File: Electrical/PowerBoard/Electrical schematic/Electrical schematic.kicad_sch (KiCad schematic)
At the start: 8 parts, among them J1 S4B-XH-SM4-TB, J2 XT60PW-M, J3 XT60PW-M, J4 2171750001, J5 XT60PW-M, U4 TMUX1204DGSR

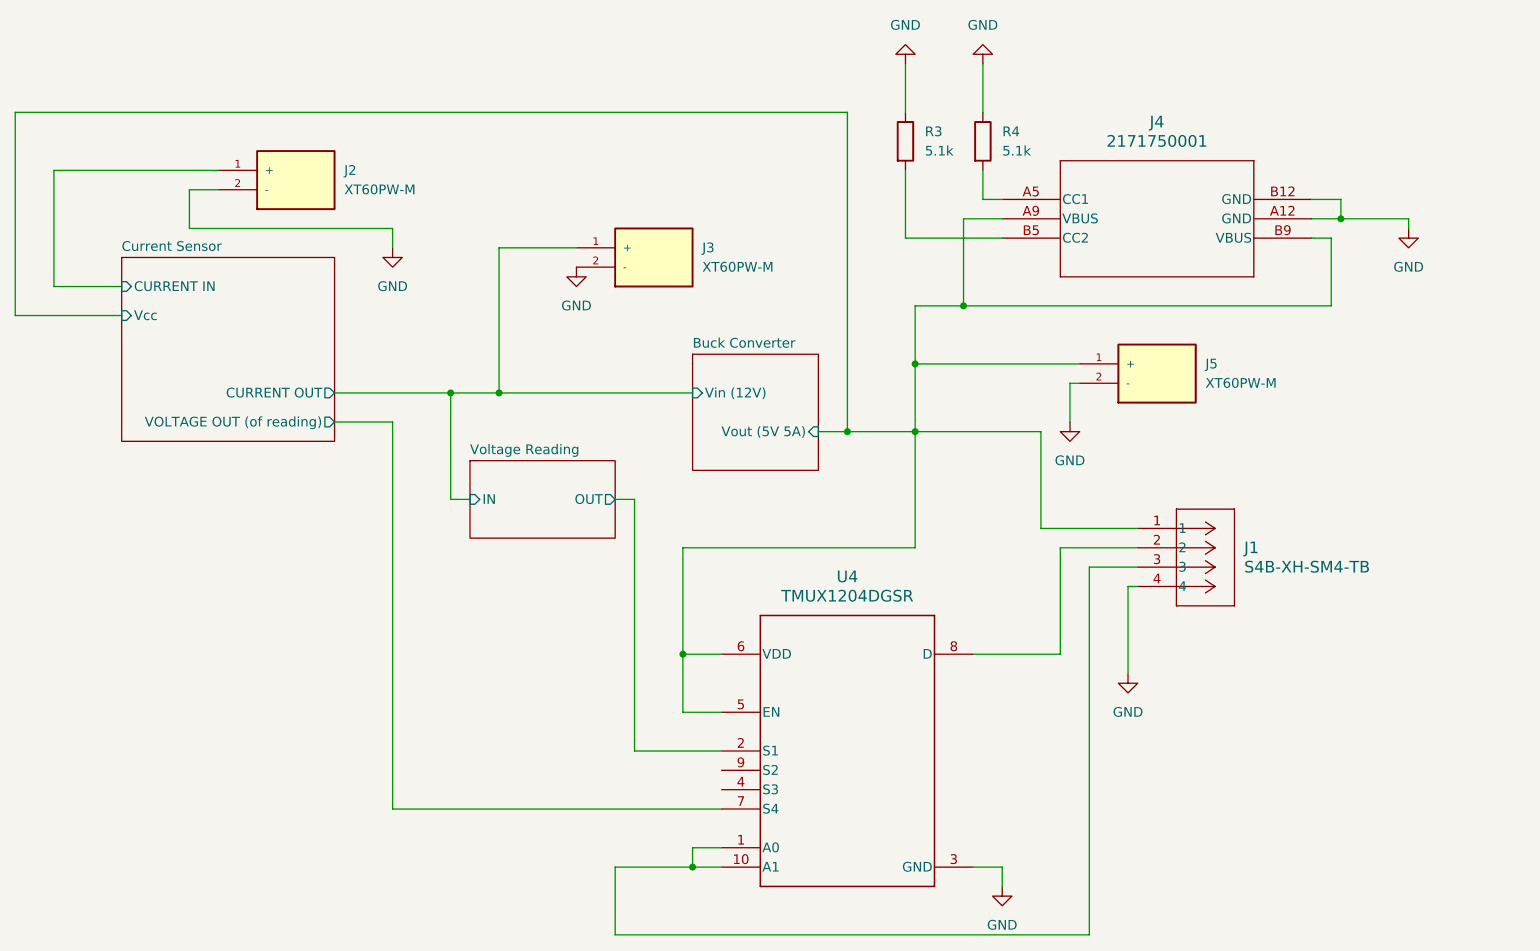
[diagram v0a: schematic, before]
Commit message: new mux/usbA
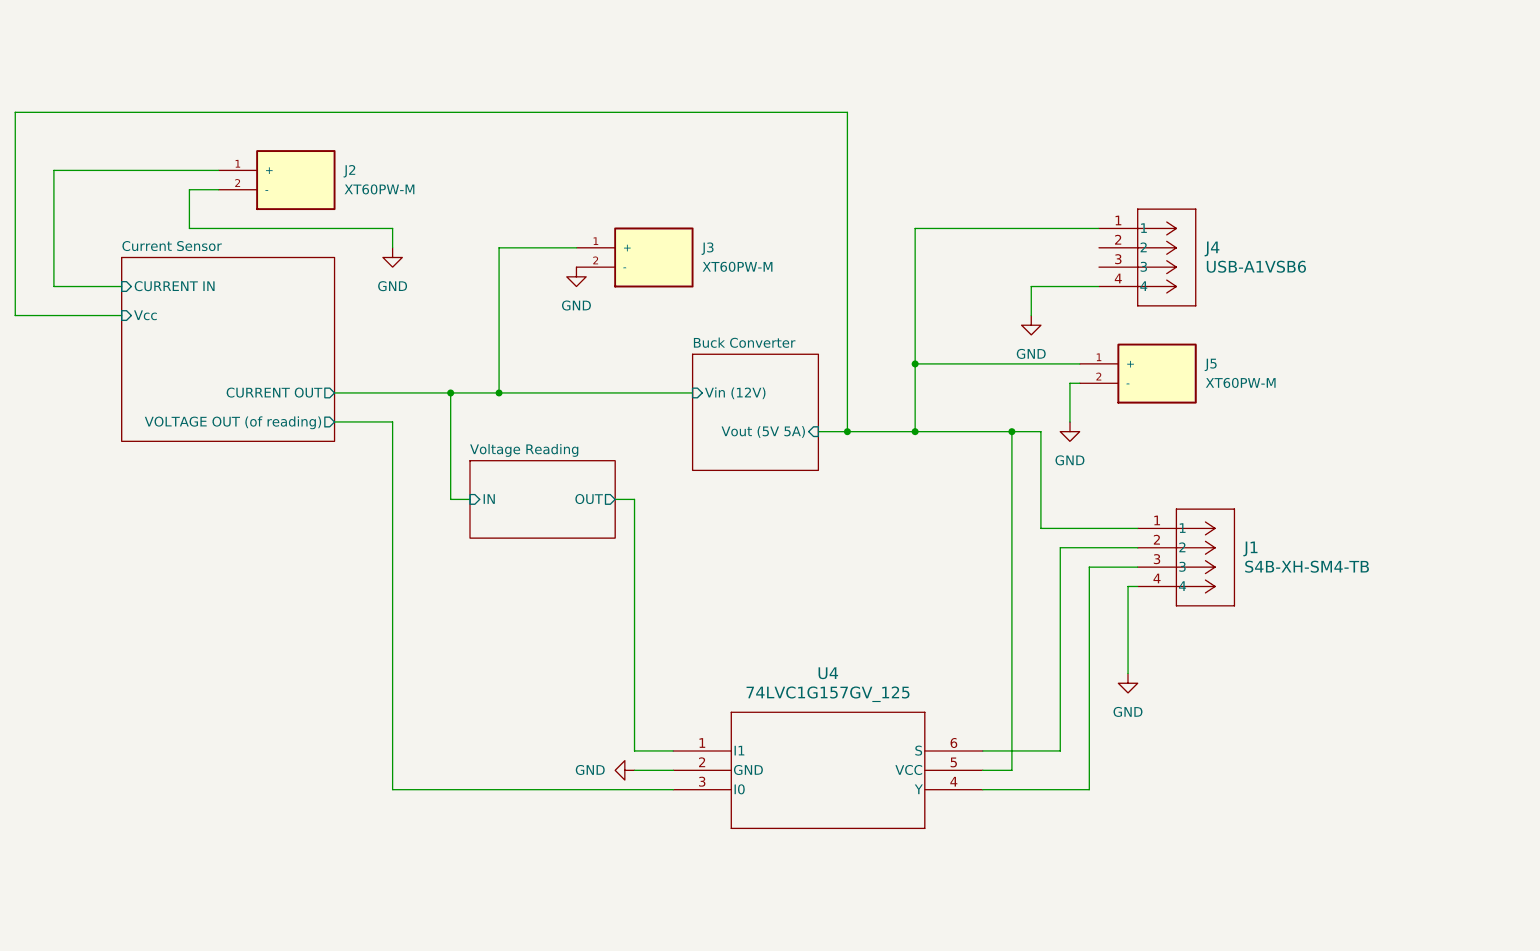
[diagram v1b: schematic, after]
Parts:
- removed J4: 2171750001, 2171750001_MOL, symbol 2025-01-31_02-22-25:2171750001
- removed R3, R4: 5.1k, Resistor_SMD:R_0805_2012Metric_Pad1.20x1.40mm_HandSolder, symbol Device:R
- removed U4: TMUX1204DGSR, DGS0010A-IPC_A, symbol 2025-01-28_22-42-53:TMUX1204DGSR
- added J4: USB-A1VSB6, CONN4_USB-A1VSB6_OST, symbol 2025-02-22_16-27-45:USB-A1VSB6
- added U4: 74LVC1G157GV_125, TSOP6_SOT457_NEX, symbol 2025-02-22_16-12-17:74LVC1G157GV_125
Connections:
- net Buck Converter/Vout (5V 5A): now also J4.1, U4.5 (VCC)
- net Current Sensor/VOLTAGE OUT (of reading): now also U4.3 (I0)
- net GND: now also J4.4, U4.2 (GND)
- net Voltage Reading/OUT: now also U4.1 (I1)
- net at J1.2: now also U4.6 (S)
- net at J1.3: now also U4.4 (Y)

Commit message: rewiring to be smaller/new mux/ fixing xt60
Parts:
- added R3: 1M, Resistor_SMD:R_0805_2012Metric_Pad1.20x1.40mm_HandSolder, symbol Device:R
- added R4: 0.333M, Resistor_SMD:R_0805_2012Metric_Pad1.20x1.40mm_HandSolder, symbol Device:R
- added U3: TLV2370IDBVR, DBV6, symbol 2025-02-22_17-10-12:TLV2370IDBVR
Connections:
- net Buck Converter/Vin (12V): now also J3.2 (-), R3.1; no longer J3.1 (+)
- net Buck Converter/Vout (5V 5A): now also J5.2 (-), U3.6 (VDD); no longer J5.1 (+)
- net Current Sensor/CURRENT IN: now also J2.2 (-); no longer J2.1 (+)
- net GND: now also J2.1 (+), J3.1 (+), J5.1 (+), R4.2, U3.2 (GND); no longer J2.2 (-), J3.2 (-), J5.2 (-)
- net Voltage Reading/OUT: no longer names the net of U4.1 (I1)
- net Voltage Reading/OUT: now also U3.1 (OUT), U3.4 (IN-)
- new net: R3.2, R4.1, U3.3 (IN+)
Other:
- removed sheet Voltage Reading

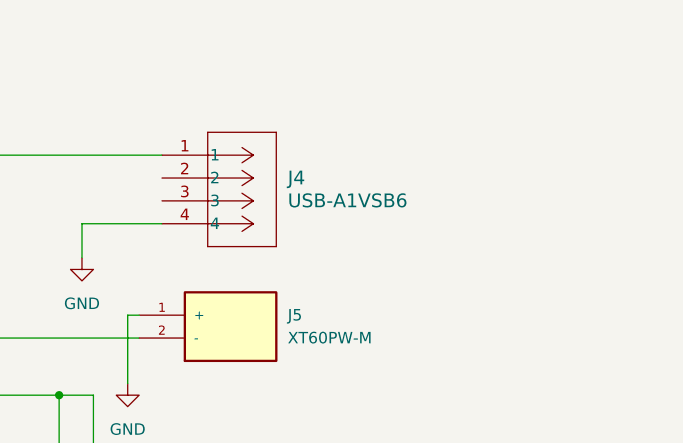
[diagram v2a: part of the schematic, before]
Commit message: adding horizontal surface mount usba
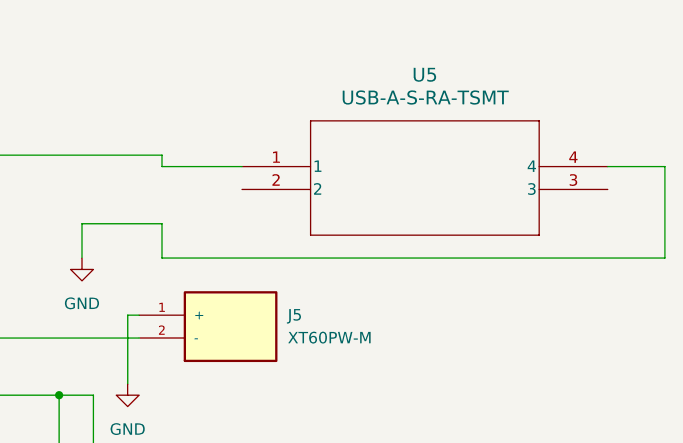
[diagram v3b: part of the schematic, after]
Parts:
- removed J4: USB-A1VSB6, CONN4_USB-A1VSB6_OST, symbol 2025-02-22_16-27-45:USB-A1VSB6
- added U5: USB-A-S-RA-TSMT, USB-A-S-RA-TSMT_ADM, symbol 2025-02-23_03-18-15:USB-A-S-RA-TSMT
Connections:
- net Buck Converter/Vout (5V 5A): now also U5.1
- net GND: now also U5.4
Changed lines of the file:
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@@
+	(wire
+		(pts
+			(xy 209.55 72.39) (xy 200.66 72.39)
+		)
+		(stroke
+			(width 0)
+			(type default)
+		)
+	)
 	(wire
 		(pts
@@
 	(wire
 		(pts
+			(xy 200.66 72.39) (xy 200.66 71.12)
+		)
+		(stroke
+			(width 0)
+			(type default)
+		)
+	)
+	(wire
+		(pts
 			(xy 74.93 128.27) (xy 74.93 124.46)
 		)
@@
 	(wire
 		(pts
+			(xy 250.19 72.39) (xy 256.54 72.39)
+		)
+		(stroke
+			(width 0)
+			(type default)
+		)
+	)
+	(wire
+		(pts
 			(xy 107.95 73.66) (xy 107.95 71.12)
 		)
@@
 	(wire
 		(pts
+			(xy 256.54 82.55) (xy 200.66 82.55)
+		)
+		(stroke
+			(width 0)
+			(type default)
+		)
+	)
+	(wire
+		(pts
 			(xy 189.23 97.79) (xy 189.23 142.24)
 		)
@@
 		(pts
 			(xy 77.47 135.89) (xy 77.47 125.73)
+		)
+		(stroke
+			(width 0)
+			(type default)
+		)
+	)
+	(wire
+		(pts
+			(xy 256.54 72.39) (xy 256.54 82.55)
+		)
+		(stroke
+			(width 0)
+			(type default)
+		)
+	)
+	(wire
+		(pts
+			(xy 200.66 82.55) (xy 200.66 78.74)
 		)
 		(stroke
@@
 	)
 	(symbol
+		(lib_id "2025-02-23_03-18-15:USB-A-S-RA-TSMT")
+		(at 209.55 72.39 0)
+		(unit 1)
+		(exclude_from_sim no)
+		(in_bom yes)
+		(on_board yes)
+		(dnp no)
+		(fields_autoplaced yes)
+		(property "Reference" "U5"
+			(at 229.87 62.23 0)
+			(effects
+				(font
+					(size 1.524 1.524)
+				)
+			)
+		)
+		(property "Value" "USB-A-S-RA-TSMT"
+			(at 229.87 64.77 0)
+			(effects
+				(font
+					(size 1.524 1.524)
+				)
+			)
+		)
+		(property "Footprint" "USB-A-S-RA-TSMT_ADM"
+			(at 209.55 72.39 0)
+			(effects
+				(font
+					(size 1.27 1.27)
+					(italic yes)
+				)
+				(hide yes)
+			)
+		)
+		(property "Datasheet" "USB-A-S-RA-TSMT"
+			(at 209.55 72.39 0)
+			(effects
+				(font
+					(size 1.27 1.27)
+					(italic yes)
+				)
+				(hide yes)
+			)
+		)
+		(property "Description" ""
+			(at 209.55 72.39 0)
+			(effects
+				(font
+					(size 1.27 1.27)
+				)
+				(hide yes)
+			)
+		)
+		(pin "1"
+		)
+		(pin "2"
+		)
+		(pin "4"
+		)
+		(pin "3"
+		)
+		(instances
+			(project ""
+				(path "/f95f296f-a4bf-4952-bdc7-66087a6cc347"
+					(reference "U5")
+					(unit 1)
+				)
+			)
+		)
+	)
+	(symbol
 		(lib_id "power:GND")
 		(at 191.77 82.55 0)
@@
 					(unit 1)
 				)
-			)
-		)
-	)
-	(symbol
-		(lib_id "2025-02-22_16-27-45:USB-A1VSB6")
-		(at 210.82 76.2 0)
-		(unit 1)
-		(exclude_from_sim no)
-		(in_bom yes)
-		(on_board yes)
-		(dnp no)
-		(fields_autoplaced yes)
-		(property "Reference" "J4"
-			(at 214.63 73.6599 0)
-			(effects
-				(font
-					(size 1.524 1.524)
-				)
-				(justify left)
-			)
-		)
-		(property "Value" "USB-A1VSB6"
-			(at 214.63 76.1999 0)
-			(effects
-				(font
-					(size 1.524 1.524)
-				)
-				(justify left)
-			)
-		)
-		(property "Footprint" "CONN4_USB-A1VSB6_OST"
-			(at 210.82 76.2 0)
-			(effects
-				(font
-					(size 1.27 1.27)
-					(italic yes)
-				)
-				(hide yes)
-			)
-		)
-		(property "Datasheet" "USB-A1VSB6"
-			(at 210.82 76.2 0)
-			(effects
-				(font
-					(size 1.27 1.27)
-					(italic yes)
-				)
-				(hide yes)
-			)
-		)
-		(property "Description" ""
-			(at 210.82 76.2 0)
-			(effects
-				(font
-					(size 1.27 1.27)
-				)
-				(hide yes)
-			)
-		)
-		(pin "3"
-		)
-		(pin "4"
-		)
-		(pin "2"
-		)
-		(pin "1"
-		)
-		(instances
-			(project ""
-				(path "/f95f296f-a4bf-4952-bdc7-66087a6cc347"
-					(reference "J4")
-					(unit 1)
-				)

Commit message: finished
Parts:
- J1: footprint CONN4_S4B-XH_JST -> Connector_JST:JST_XH_B4B-XH-A_1x04_P2.50mm_Vertical
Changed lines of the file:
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@@
 			)
 		)
-		(property "Footprint" "CONN4_S4B-XH_JST"
+		(property "Footprint" "Connector_JST:JST_XH_B4B-XH-A_1x04_P2.50mm_Vertical"
 			(at 205.74 110.49 0)
 			(effects

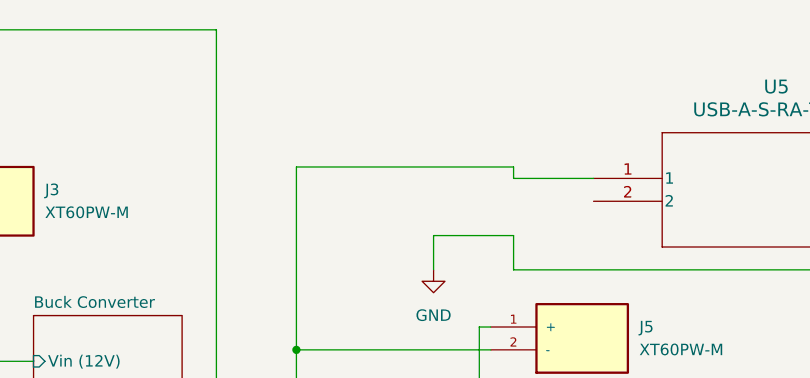
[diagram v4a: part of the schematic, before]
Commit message: Buck Board Version 1
Added capacitor for Pi rail
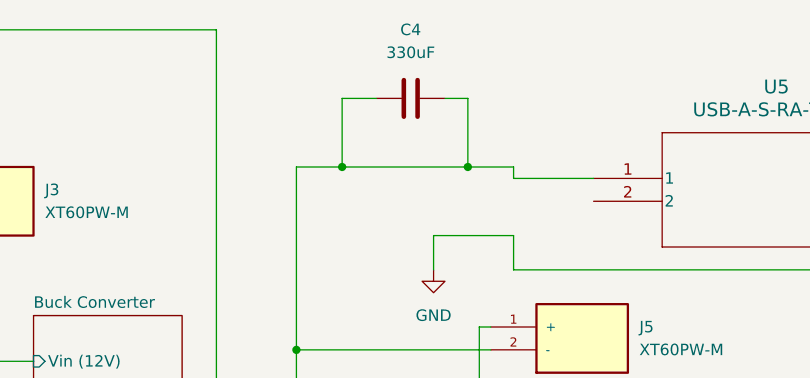
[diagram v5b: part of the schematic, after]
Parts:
- added C4: 330uF, Capacitor_SMD:C_0805_2012Metric_Pad1.18x1.45mm_HandSolder, symbol Device:C
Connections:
- net Buck Converter/Vout (5V 5A): now also C4.1, C4.2
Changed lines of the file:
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@@
+	)
+	(junction
+		(at 181.61 71.12)
+		(diameter 0)
+		(color 0 0 0 0)
 	)
 	(junction
@@
 		(color 0 0 0 0)
 	)
+	(junction
+		(at 195.58 71.12)
+		(diameter 0)
+		(color 0 0 0 0)
+	)
 	(wire
 		(pts
@@
 	(wire
 		(pts
-			(xy 200.66 71.12) (xy 176.53 71.12)
+			(xy 200.66 71.12) (xy 195.58 71.12)
 		)
 		(stroke
@@
 	(wire
 		(pts
+			(xy 181.61 71.12) (xy 176.53 71.12)
+		)
+		(stroke
+			(width 0)
+			(type default)
+		)
+	)
+	(wire
+		(pts
 			(xy 135.89 139.7) (xy 144.78 139.7)
 		)
@@
 	(wire
 		(pts
+			(xy 185.42 63.5) (xy 181.61 63.5)
+		)
+		(stroke
+			(width 0)
+			(type default)
+		)
+	)
+	(wire
+		(pts
 			(xy 204.47 129.54) (xy 204.47 118.11)
 		)
@@
 	(wire
 		(pts
+			(xy 181.61 63.5) (xy 181.61 71.12)
+		)
+		(stroke
+			(width 0)
+			(type default)
+		)
+	)
+	(wire
+		(pts
 			(xy 193.04 97.79) (xy 193.04 110.49)
 		)
@@
 	(wire
 		(pts
+			(xy 193.04 63.5) (xy 195.58 63.5)
+		)
+		(stroke
+			(width 0)
+			(type default)
+		)
+	)
+	(wire
+		(pts
 			(xy 189.23 97.79) (xy 176.53 97.79)
 		)
@@
 	(wire
 		(pts
+			(xy 195.58 71.12) (xy 181.61 71.12)
+		)
+		(stroke
+			(width 0)
+			(type default)
+		)
+	)
+	(wire
+		(pts
 			(xy 80.01 135.89) (xy 77.47 135.89)
 		)
@@
 		(pts
 			(xy 135.89 139.7) (xy 135.89 130.81)
+		)
+		(stroke
+			(width 0)
+			(type default)
+		)
+	)
+	(wire
+		(pts
+			(xy 195.58 63.5) (xy 195.58 71.12)
 		)
 		(stroke
@@
 					(unit 1)
 				)
+			)
+		)
+	)
+	(symbol
+		(lib_id "Device:C")
+		(at 189.23 63.5 90)
+		(unit 1)
+		(exclude_from_sim no)
+		(in_bom yes)
+		(on_board yes)
+		(dnp no)
+		(fields_autoplaced yes)
+		(property "Reference" "C4"
+			(at 189.23 55.88 90)
+			(effects
+				(font
+					(size 1.27 1.27)
+				)
+			)
+		)
+		(property "Value" "330uF"
+			(at 189.23 58.42 90)
+			(effects
+				(font
+					(size 1.27 1.27)
+				)
+			)
+		)
+		(property "Footprint" "Capacitor_SMD:C_0805_2012Metric_Pad1.18x1.45mm_HandSolder"
+			(at 193.04 62.5348 0)
+			(effects
+				(font
+					(size 1.27 1.27)
+				)
+				(hide yes)
+			)
+		)
+		(property "Datasheet" "~"
+			(at 189.23 63.5 0)
+			(effects
+				(font
+					(size 1.27 1.27)
+				)
+				(hide yes)
+			)
+		)
+		(property "Description" "Unpolarized capacitor"
+			(at 189.23 63.5 0)
+			(effects
+				(font
+					(size 1.27 1.27)
+				)
+				(hide yes)
+			)
+		)
+		(pin "1"
+		)
+		(pin "2"
+		)
+		(instances
+			(project "Electrical schematic"
+				(path "/f95f296f-a4bf-4952-bdc7-66087a6cc347"
+					(reference "C4")
+					(unit 1)
+				)

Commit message: powerboard design
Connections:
- net Buck Converter/Vout (5V 5A): no longer C4.1
- net GND: now also C4.1
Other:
- moved on the sheet: C4
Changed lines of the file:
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@@
+	)
+	(junction
+		(at 195.58 78.74)
+		(diameter 0)
+		(color 0 0 0 0)
 	)
 	(junction
@@
 	)
 	(junction
-		(at 181.61 71.12)
+		(at 195.58 71.12)
 		(diameter 0)
 		(color 0 0 0 0)
@@
 		(color 0 0 0 0)
 	)
-	(junction
-		(at 195.58 71.12)
-		(diameter 0)
-		(color 0 0 0 0)
-	)
 	(wire
 		(pts
@@
 	(wire
 		(pts
-			(xy 191.77 78.74) (xy 200.66 78.74)
+			(xy 191.77 78.74) (xy 195.58 78.74)
 		)
 		(stroke
@@
 	(wire
 		(pts
-			(xy 200.66 71.12) (xy 195.58 71.12)
-		)
-		(stroke
-			(width 0)
-			(type default)
-		)
-	)
-	(wire
-		(pts
 			(xy 157.48 110.49) (xy 157.48 128.27)
 		)
@@
 	(wire
 		(pts
-			(xy 181.61 71.12) (xy 176.53 71.12)
+			(xy 176.53 71.12) (xy 195.58 71.12)
 		)
 		(stroke
@@
 	(wire
 		(pts
-			(xy 185.42 63.5) (xy 181.61 63.5)
-		)
-		(stroke
-			(width 0)
-			(type default)
-		)
-	)
-	(wire
-		(pts
 			(xy 204.47 129.54) (xy 204.47 118.11)
 		)
@@
 	(wire
 		(pts
-			(xy 181.61 63.5) (xy 181.61 71.12)
-		)
-		(stroke
-			(width 0)
-			(type default)
-		)
-	)
-	(wire
-		(pts
 			(xy 193.04 97.79) (xy 193.04 110.49)
 		)
@@
 	(wire
 		(pts
+			(xy 195.58 78.74) (xy 200.66 78.74)
+		)
+		(stroke
+			(width 0)
+			(type default)
+		)
+	)
+	(wire
+		(pts
 			(xy 121.92 76.2) (xy 132.08 76.2)
 		)
@@
 	(wire
 		(pts
-			(xy 193.04 63.5) (xy 195.58 63.5)
-		)
-		(stroke
-			(width 0)
-			(type default)
-		)
-	)
-	(wire
-		(pts
 			(xy 189.23 97.79) (xy 176.53 97.79)
 		)
@@
 	(wire
 		(pts
+			(xy 195.58 71.12) (xy 200.66 71.12)
+		)
+		(stroke
+			(width 0)
+			(type default)
+		)
+	)
+	(wire
+		(pts
 			(xy 63.5 66.04) (xy 63.5 78.74)
 		)
@@
 	(wire
 		(pts
-			(xy 195.58 71.12) (xy 181.61 71.12)
-		)
-		(stroke
-			(width 0)
-			(type default)
-		)
-	)
-	(wire
-		(pts
 			(xy 80.01 135.89) (xy 77.47 135.89)
 		)
@@
 		(pts
 			(xy 135.89 139.7) (xy 135.89 130.81)
-		)
-		(stroke
-			(width 0)
-			(type default)
-		)
-	)
-	(wire
-		(pts
-			(xy 195.58 63.5) (xy 195.58 71.12)
 		)
 		(stroke
@@
 	(symbol
 		(lib_id "Device:C")
-		(at 189.23 63.5 90)
+		(at 195.58 74.93 180)
 		(unit 1)
 		(exclude_from_sim no)
@@
 		(fields_autoplaced yes)
 		(property "Reference" "C4"
-			(at 189.23 55.88 90)
-			(effects
-				(font
-					(size 1.27 1.27)
-				)
+			(at 199.39 73.6599 0)
+			(effects
+				(font
+					(size 1.27 1.27)
+				)
+				(justify right)
 			)
 		)
 		(property "Value" "330uF"
-			(at 189.23 58.42 90)
-			(effects
-				(font
-					(size 1.27 1.27)
-				)
+			(at 199.39 76.1999 0)
+			(effects
+				(font
+					(size 1.27 1.27)
+				)
+				(justify right)
 			)
 		)
 		(property "Footprint" "Capacitor_SMD:C_0805_2012Metric_Pad1.18x1.45mm_HandSolder"
-			(at 193.04 62.5348 0)
+			(at 194.6148 71.12 0)
 			(effects
 				(font
@@
 		)
 		(property "Datasheet" "~"
-			(at 189.23 63.5 0)
+			(at 195.58 74.93 0)
 			(effects
 				(font
@@
 		)
 		(property "Description" "Unpolarized capacitor"
-			(at 189.23 63.5 0)
-			(effects
-				(font
+			(at 195.58 74.93 0)
+			(effects
+				(font
